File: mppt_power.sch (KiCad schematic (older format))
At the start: 33 parts

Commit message: Minor schematic update
Signed-off-by: Patrick Rudolph <siro@das-labor.org>
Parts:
- removed U? (x2): SFH617A-2X019T, Package_DIP:SMDIP-4_W7.62mm, symbol Isolator:SFH617A-2X019T
- added J?: Conn_01x02_Male, symbol Connector:Conn_01x02_Male
- added R?: 470, symbol Device:R
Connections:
- net GND: now also U?.3
- net at A?.6 (D3), D?.2 (A), R?.1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: now also U?.4
- net at U?.1: now also R?.1
- net at U?.2: now also J?.2 (Pin_2)
- new net: J?.1 (Pin_1), R?.2
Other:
- note added: "external force disable"
- note added: "sense low power"
- note added: "sense output no load"
- moved on the sheet: U?
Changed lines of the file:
@@
-$Comp
-L Isolator:SFH617A-2X019T U?
-U 1 1 5D920DD0
-P 6950 2600
-F 0 "U?" H 6950 2925 50  0000 C CNN
-F 1 "SFH617A-2X019T" H 6950 2834 50  0000 C CNN
-F 2 "Package_DIP:SMDIP-4_W7.62mm" H 6950 2300 50  0001 C CNN
-F 3 "http://www.vishay.com/docs/83740/sfh617a.pdf" H 6600 2900 50  0001 C CNN
-	1    6950 2600
-	1    0    0    -1
-$EndComp
-$Comp
-L Isolator:SFH617A-2X019T U?
-U 1 1 5D921C12
-P 6950 3050
-F 0 "U?" H 6950 3375 50  0000 C CNN
-F 1 "SFH617A-2X019T" H 6950 3284 50  0000 C CNN
-F 2 "Package_DIP:SMDIP-4_W7.62mm" H 6950 2750 50  0001 C CNN
-F 3 "http://www.vishay.com/docs/83740/sfh617a.pdf" H 6600 3350 50  0001 C CNN
-	1    6950 3050
-	1    0    0    -1
-$EndComp
 $Comp
 L Isolator:SFH617A-2X019T U?
 U 1 1 5D9224BB
-P 8750 3300
-F 0 "U?" H 8750 3625 50  0000 C CNN
-F 1 "SFH617A-2X019T" H 8750 3534 50  0000 C CNN
-F 2 "Package_DIP:SMDIP-4_W7.62mm" H 8750 3000 50  0001 C CNN
-F 3 "http://www.vishay.com/docs/83740/sfh617a.pdf" H 8400 3600 50  0001 C CNN
-	1    8750 3300
+P 7950 2950
+F 0 "U?" H 7950 3275 50  0000 C CNN
+F 1 "SFH617A-2X019T" H 7950 3184 50  0000 C CNN
+F 2 "Package_DIP:SMDIP-4_W7.62mm" H 7950 2650 50  0001 C CNN
+F 3 "http://www.vishay.com/docs/83740/sfh617a.pdf" H 7600 3250 50  0001 C CNN
+	1    7950 2950
 	1    0    0    -1
 $EndComp
@@
 	4550 2200 4550 2400
 Connection ~ 4550 2200
+$Comp
+L power:GND #PWR?
+U 1 1 5D65C100
+P 8350 3150
+F 0 "#PWR?" H 8350 2900 50  0001 C CNN
+F 1 "GND" H 8355 2977 50  0000 C CNN
+F 2 "" H 8350 3150 50  0001 C CNN
+F 3 "" H 8350 3150 50  0001 C CNN
+	1    8350 3150
+	1    0    0    -1
+$EndComp
+Wire Wire Line
+	8250 3050 8350 3050
+Wire Wire Line
+	8350 3050 8350 3150
+$Comp
+L Device:R R?
+U 1 1 5D662C62
+P 7350 2850
+F 0 "R?" V 7143 2850 50  0000 C CNN
+F 1 "470" V 7234 2850 50  0000 C CNN
+F 2 "" V 7280 2850 50  0001 C CNN
+F 3 "~" H 7350 2850 50  0001 C CNN
+F 4 "PMR18EZPJU7L0" V 7350 2850 50  0001 C CNN "Recommended"
+	1    7350 2850
+	0    1    1    0
+$EndComp
+Wire Wire Line
+	7650 2850 7500 2850
+Wire Wire Line
+	7650 3050 7050 3050
+Text Notes 7350 1850 1    50   ~ 0
+sense low power
+Text Notes 8200 2250 0    50   ~ 0
+sense output no load
+$Comp
+L Connector:Conn_01x02_Male J?
+U 1 1 5D681563
+P 6600 2900
+F 0 "J?" H 6708 3081 50  0000 C CNN
+F 1 "Conn_01x02_Male" H 6708 2990 50  0000 C CNN
+F 2 "" H 6600 2900 50  0001 C CNN
+F 3 "~" H 6600 2900 50  0001 C CNN
+	1    6600 2900
+	1    0    0    -1
+$EndComp
+Wire Wire Line
+	6800 3000 7050 3000
+Wire Wire Line
+	7050 3000 7050 3050
+Wire Wire Line
+	7200 2850 7050 2850
+Wire Wire Line
+	7050 2850 7050 2900
+Wire Wire Line
+	7050 2900 6800 2900
+Text Notes 6850 3200 0    50   ~ 0
+external force disable
+Wire Wire Line
+	8250 2850 8350 2850
+Wire Wire Line
+	8350 2850 8350 2400
+Wire Wire Line
+	8350 2400 7850 2400
+Wire Wire Line
+	7850 2400 7850 1700
 $EndSCHEMATC

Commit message: Huge schematic and documentation update
Signed-off-by: Patrick Rudolph <siro@das-labor.org>
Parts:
- removed C?: 100n, symbol Device:C_Small
- removed U?: MCP4725, symbol MICROCHIP:MCP4725
- added D?: LED, symbol Device:LED
- added D?: BZT52B6V8, Diode_SMD:D_SOD-123, symbol Device:D_Zener_Small
- added Q?: MMBTA42, symbol Device:Q_NPN_BCE
- added R?: 1k, symbol Device:R
- added R?: 130, symbol Device:R
- added R?: 100k, symbol Device:R
- added R? (x3): 0, symbol Device:R
- L?: footprint (none) -> Inductor_THT:L_Toroid_Vertical_L31.8mm_W15.9mm_P13.50mm_Bourns_5700
- L?: value L_Core_Ferrite_Coupled -> SC-07-276JH
- R? (x3): value 0,007 -> 0,01
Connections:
- net +3V3: now also R?.2; no longer A?.17 (3V3)
- net GND: now also D?.1 (K), D?.2 (A)
- net VBUS: now also R?.1, R?.2; no longer A?.30 (VIN)
- net V_IN_CS: now reaches L?.2, R?.1, R?.1, R?.1, R?.2
- net V_IN_CS: now also R?.2
- net at A?.13 (D10): now also R?.2
- new net: A?.17 (3V3), R?.1
- new net: A?.30 (VIN), R?.1
- new net: D?.2 (A), R?.1
- new net: Q?.3 (E), R?.2
- new net: D?.1 (K), Q?.1 (B), R?.1
- new net: Q?.2 (C), R?.1, R?.2
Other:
- note added: "16,5A max"
- note added: "55mV full resolution"
- note added: "bootstrap and emergency logic supply"
- note added: "debug LED"
- note added: "disable main SMPS"
- note removed: "23,5A max"
- note removed: "Adjustable current limit"
- note removed: "address: 1100000"
- moved on the sheet: C?, L?

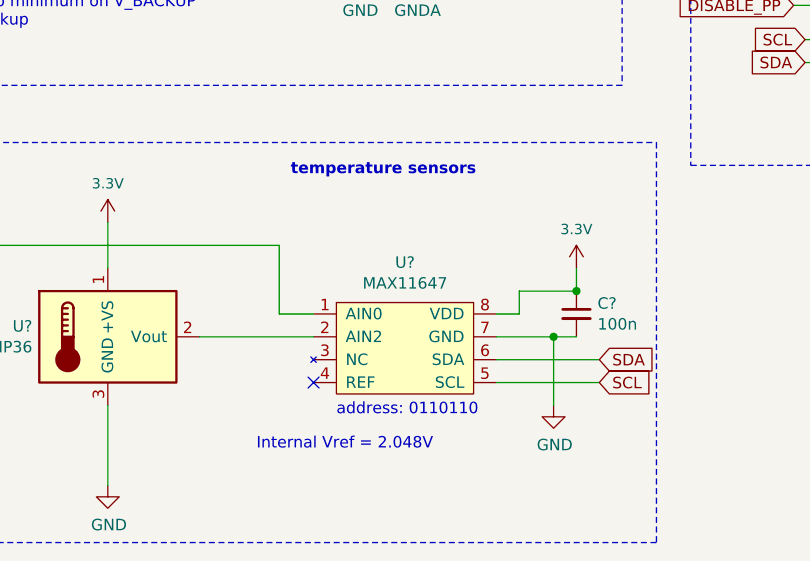
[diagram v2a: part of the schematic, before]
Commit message: Add more packages
Signed-off-by: Patrick Rudolph <siro@das-labor.org>
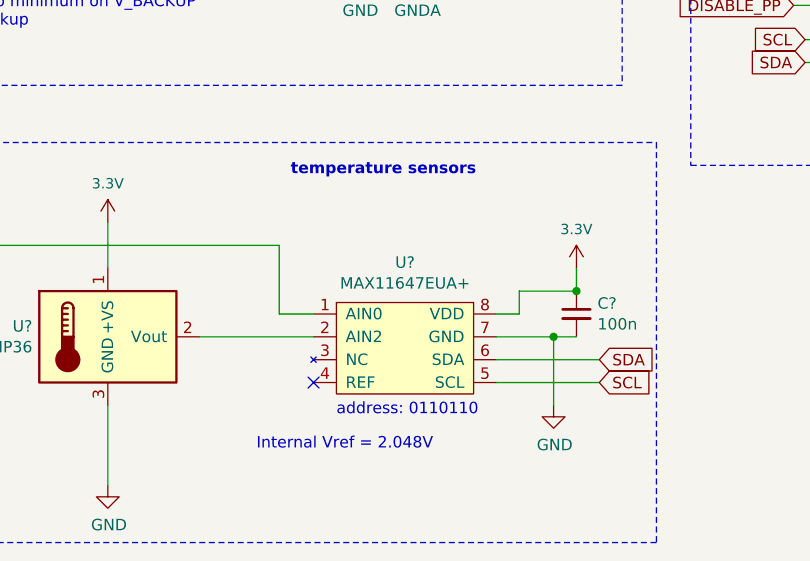
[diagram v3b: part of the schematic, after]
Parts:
- C? (x3): footprint (none) -> Capacitor_SMD:C_0805_2012Metric
- C? (x2): footprint (none) -> Capacitor_SMD:C_0603_1608Metric
- C?: footprint (none) -> Resistor_SMD:R_0805_2012Metric
- R? (x3): footprint (none) -> Resistor_SMD:R_0612_1632Metric
- R? (x2): footprint (none) -> Resistor_SMD:R_0603_1608Metric
- U?: footprint (none) -> Package_SO:MSOP-10_3x3mm_P0.5mm
- U?: value MAX11647 -> MAX11647EUA+; footprint (none) -> Package_SO:MSOP-8_3x3mm_P0.65mm
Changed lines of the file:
@@
 EESchema Schematic File Version 4
 LIBS:mppt_power-cache
-EELAYER 29 0
+EELAYER 30 0
 EELAYER END
 $Descr A4 11693 8268
@@
 F 0 "U?" H 4425 3815 50  0000 C CNN
 F 1 "MAX9611" H 4425 3724 50  0000 C CNN
-F 2 "" H 4400 3100 50  0001 C CNN
+F 2 "Package_SO:MSOP-10_3x3mm_P0.5mm" H 4400 3100 50  0001 C CNN
 F 3 "https://datasheets.maximintegrated.com/en/ds/MAX9611-MAX9612.pdf" H 4400 3100 50  0001 C CNN
 	1    4400 3100
@@
 F 0 "R?" V 4043 1350 50  0000 C CNN
 F 1 "0,01" V 4134 1350 50  0000 C CNN
-F 2 "" V 4180 1350 50  0001 C CNN
+F 2 "Resistor_SMD:R_0612_1632Metric" V 4180 1350 50  0001 C CNN
 F 3 "~" H 4250 1350 50  0001 C CNN
 F 4 "PMR18EZPJU7L0" V 4250 1350 50  0001 C CNN "Recommended"
@@
 F 0 "C?" H 2192 1346 50  0000 L CNN
 F 1 "100n" H 2192 1255 50  0000 L CNN
-F 2 "" H 2100 1300 50  0001 C CNN
+F 2 "Capacitor_SMD:C_0805_2012Metric" H 2100 1300 50  0001 C CNN
 F 3 "~" H 2100 1300 50  0001 C CNN
 	1    2100 1300
@@
 F 0 "C?" H 2192 1646 50  0000 L CNN
 F 1 "100n" H 2192 1555 50  0000 L CNN
-F 2 "" H 2100 1600 50  0001 C CNN
+F 2 "Capacitor_SMD:C_0805_2012Metric" H 2100 1600 50  0001 C CNN
 F 3 "~" H 2100 1600 50  0001 C CNN
 	1    2100 1600
@@
 F 0 "C?" H 3442 1546 50  0000 L CNN
 F 1 "100n" H 3442 1455 50  0000 L CNN
-F 2 "" H 3350 1500 50  0001 C CNN
+F 2 "Capacitor_SMD:C_0805_2012Metric" H 3350 1500 50  0001 C CNN
 F 3 "~" H 3350 1500 50  0001 C CNN
 	1    3350 1500
@@
 F 0 "C?" H 5842 2796 50  0000 L CNN
 F 1 "100n" H 5842 2705 50  0000 L CNN
-F 2 "" H 5750 2750 50  0001 C CNN
+F 2 "Capacitor_SMD:C_0603_1608Metric" H 5750 2750 50  0001 C CNN
 F 3 "~" H 5750 2750 50  0001 C CNN
 	1    5750 2750
@@
 F 0 "R?" V 4043 1650 50  0000 C CNN
 F 1 "0,01" V 4134 1650 50  0000 C CNN
-F 2 "" V 4180 1650 50  0001 C CNN
+F 2 "Resistor_SMD:R_0612_1632Metric" V 4180 1650 50  0001 C CNN
 F 3 "~" H 4250 1650 50  0001 C CNN
 F 4 "PMR18EZPJU7L0" V 4250 1650 50  0001 C CNN "Recommended"
@@
 F 0 "R?" V 4043 1950 50  0000 C CNN
 F 1 "0,01" V 4134 1950 50  0000 C CNN
-F 2 "" V 4180 1950 50  0001 C CNN
+F 2 "Resistor_SMD:R_0612_1632Metric" V 4180 1950 50  0001 C CNN
 F 3 "~" H 4250 1950 50  0001 C CNN
 F 4 "PMR18EZPJU7L0" V 4250 1950 50  0001 C CNN "Recommended"
@@
 P 4100 6850
 F 0 "U?" H 4100 7475 50  0000 C CNN
-F 1 "MAX11647" H 4100 7384 50  0000 C CNN
-F 2 "" H 4100 6850 50  0001 C CNN
+F 1 "MAX11647EUA+" H 4100 7384 50  0000 C CNN
+F 2 "Package_SO:MSOP-8_3x3mm_P0.65mm" H 4100 6850 50  0001 C CNN
 F 3 "https://www.mouser.de/datasheet/2/256/MAX11646-MAX11647-1513342.pdf" H 4100 6850 50  0001 C CNN
 	1    4100 6850
@@
 F 0 "C?" H 4942 6496 50  0000 L CNN
 F 1 "100n" H 4942 6405 50  0000 L CNN
-F 2 "" H 4850 6450 50  0001 C CNN
+F 2 "Capacitor_SMD:C_0603_1608Metric" H 4850 6450 50  0001 C CNN
 F 3 "~" H 4850 6450 50  0001 C CNN
 	1    4850 6450
@@
 F 0 "C?" H 4342 2246 50  0000 L CNN
 F 1 "2u" H 4342 2155 50  0000 L CNN
-F 2 "" H 4250 2200 50  0001 C CNN
+F 2 "Resistor_SMD:R_0805_2012Metric" H 4250 2200 50  0001 C CNN
 F 3 "~" H 4250 2200 50  0001 C CNN
 	1    4250 2200
@@
 F 0 "R?" V 4343 2000 50  0000 C CNN
 F 1 "10" V 4434 2000 50  0000 C CNN
-F 2 "" V 4480 2000 50  0001 C CNN
+F 2 "Resistor_SMD:R_0603_1608Metric" V 4480 2000 50  0001 C CNN
 F 3 "~" H 4550 2000 50  0001 C CNN
 F 4 "PMR18EZPJU7L0" V 4550 2000 50  0001 C CNN "Recommended"
@@
 F 0 "R?" V 3693 2000 50  0000 C CNN
 F 1 "10" V 3784 2000 50  0000 C CNN
-F 2 "" V 3830 2000 50  0001 C CNN
+F 2 "Resistor_SMD:R_0603_1608Metric" V 3830 2000 50  0001 C CNN
 F 3 "~" H 3900 2000 50  0001 C CNN
 F 4 "PMR18EZPJU7L0" V 3900 2000 50  0001 C CNN "Recommended"

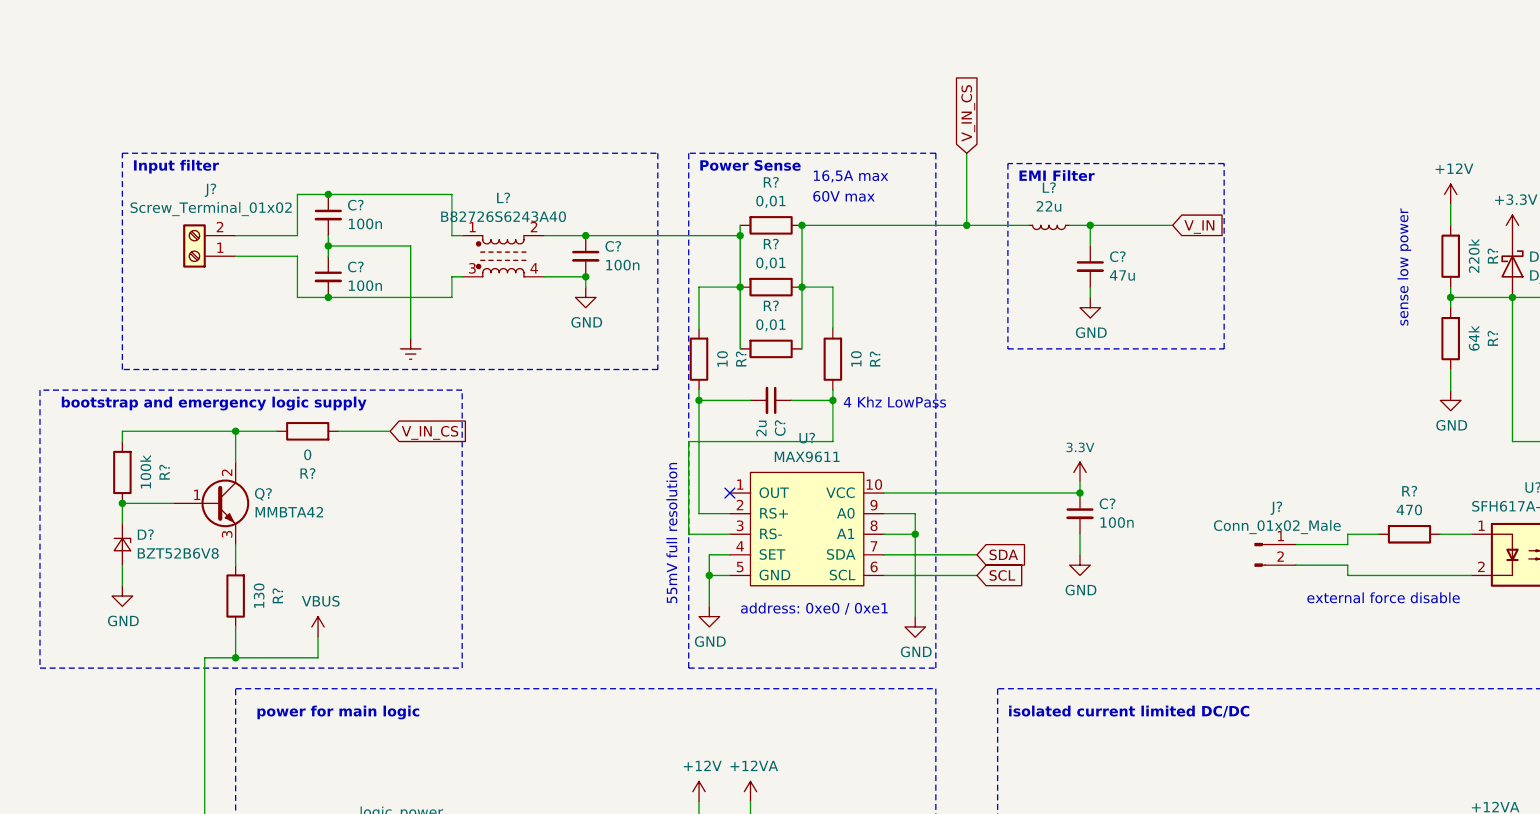
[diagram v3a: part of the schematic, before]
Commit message: Split into more schematics, add more comments
Signed-off-by: Patrick Rudolph <siro@das-labor.org>
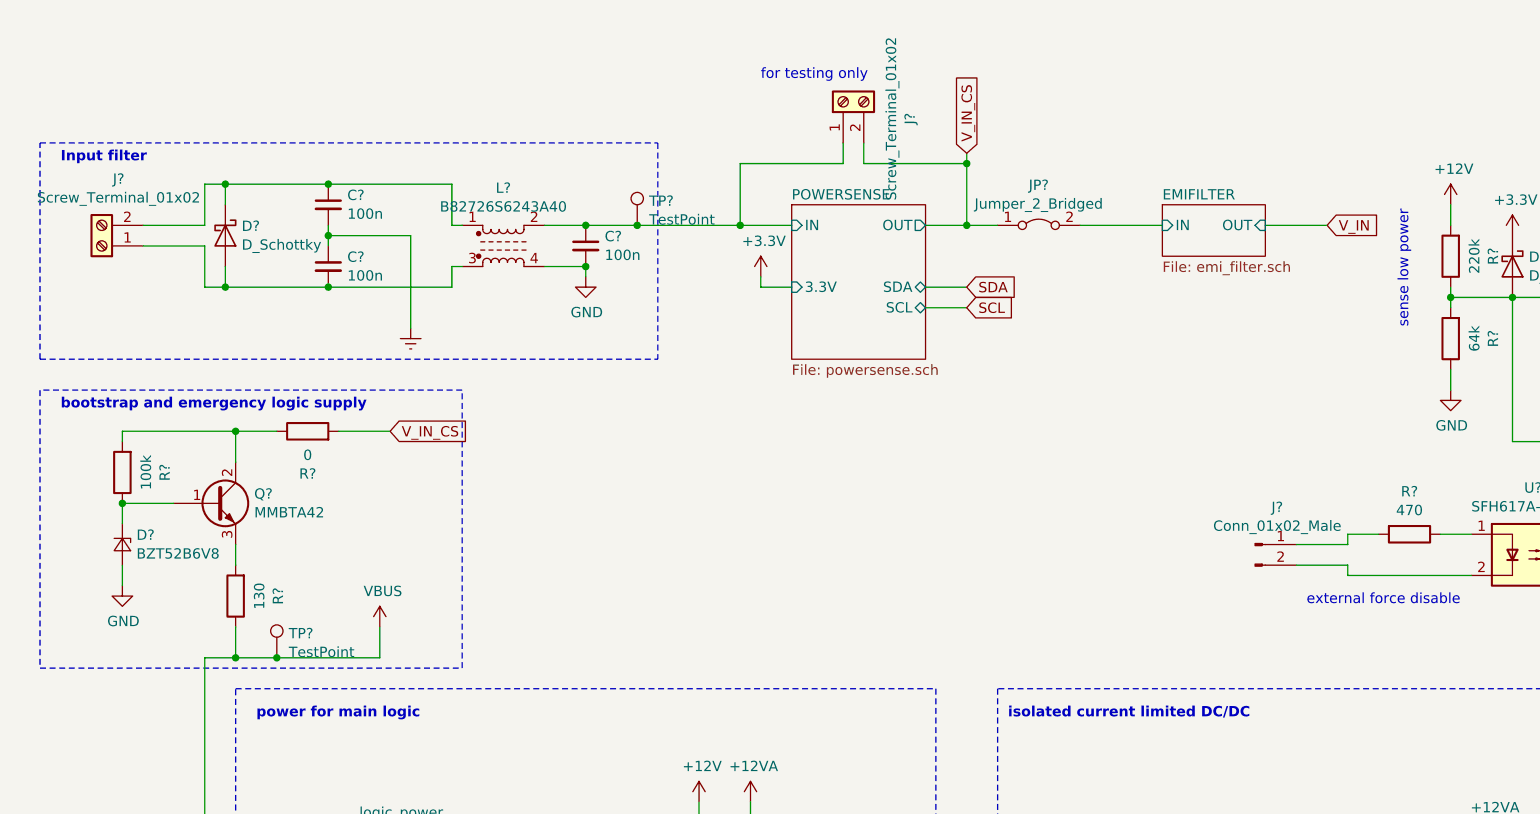
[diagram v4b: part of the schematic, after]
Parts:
- removed C?: 47u, symbol Device:C_Small
- removed C?: 100n, Capacitor_SMD:C_0603_1608Metric, symbol Device:C_Small
- removed C?: 2u, Resistor_SMD:R_0805_2012Metric, symbol Device:C_Small
- removed L?: 22u, Inductor_THT:L_Toroid_Vertical_L31.8mm_W15.9mm_P13.50mm_Bourns_5700, symbol Device:L_Small
- removed R? (x3): 0,01, Resistor_SMD:R_0612_1632Metric, symbol Device:R
- removed R? (x2): 10, Resistor_SMD:R_0603_1608Metric, symbol Device:R
- removed U?: MAX9611, Package_SO:MSOP-10_3x3mm_P0.5mm, symbol MAX:MAX9611
- added D?: D_Schottky, symbol Device:D_Schottky
- added J?: Screw_Terminal_01x02, symbol Connector:Screw_Terminal_01x02
- added JP?: Jumper_2_Bridged, symbol Jumper:Jumper_2_Bridged
- added TP? (x2): TestPoint, symbol Connector:TestPoint
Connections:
- net VBUS: now also TP?.1
- net V_IN_CS: now also J?.2 (Pin_2), JP?.1 (A)
- net POWERSENSE/IN: now reaches C?.1, L?.2
- net POWERSENSE/IN: now also J?.1 (Pin_1), TP?.1
- net at C?.1, J?.2 (Pin_2), L?.1: now also D?.1 (K)
- net at C?.2, J?.1 (Pin_1), L?.3: now also D?.2 (A)
- new net EMIFILTER/IN: JP?.2 (B)
- no-connect marks 2 -> 1
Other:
- note added: "for testing only"
- note removed: "16,5A max"
- note removed: "4 Khz LowPass"
- note removed: "55mV full resolution"
- note removed: "60V max"
- note removed: "EMI Filter"
- note removed: "Power Sense"
- note removed: "address: 0xe0 / 0xe1"
- moved on the sheet: C?, J?, L?
